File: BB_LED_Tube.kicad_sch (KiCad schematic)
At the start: 45 parts, among them U1 ESP32-WROOM-32, U2 MAX485E, U3 TPS54202DDC, U4 AP2112K-3.3

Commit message: added reverse voltage protection & more mounting holes
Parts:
- added D1: D_Small, Diode_SMD:D_SMB, symbol Device:D_Small
- added H3, H4: MountingHole, MountingHole:MountingHole_2.7mm_M2.5, symbol Mechanical:MountingHole
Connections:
- net VCC: now also D1.1 (K); no longer VCC2.1
- new net VIN: D1.2 (A), VCC2.1
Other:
- moved on the sheet: GND1, GND2, GND3, GND4, GND5, GND6, GND7, VCC1, VCC2, VCC3, VCC4, VCC5

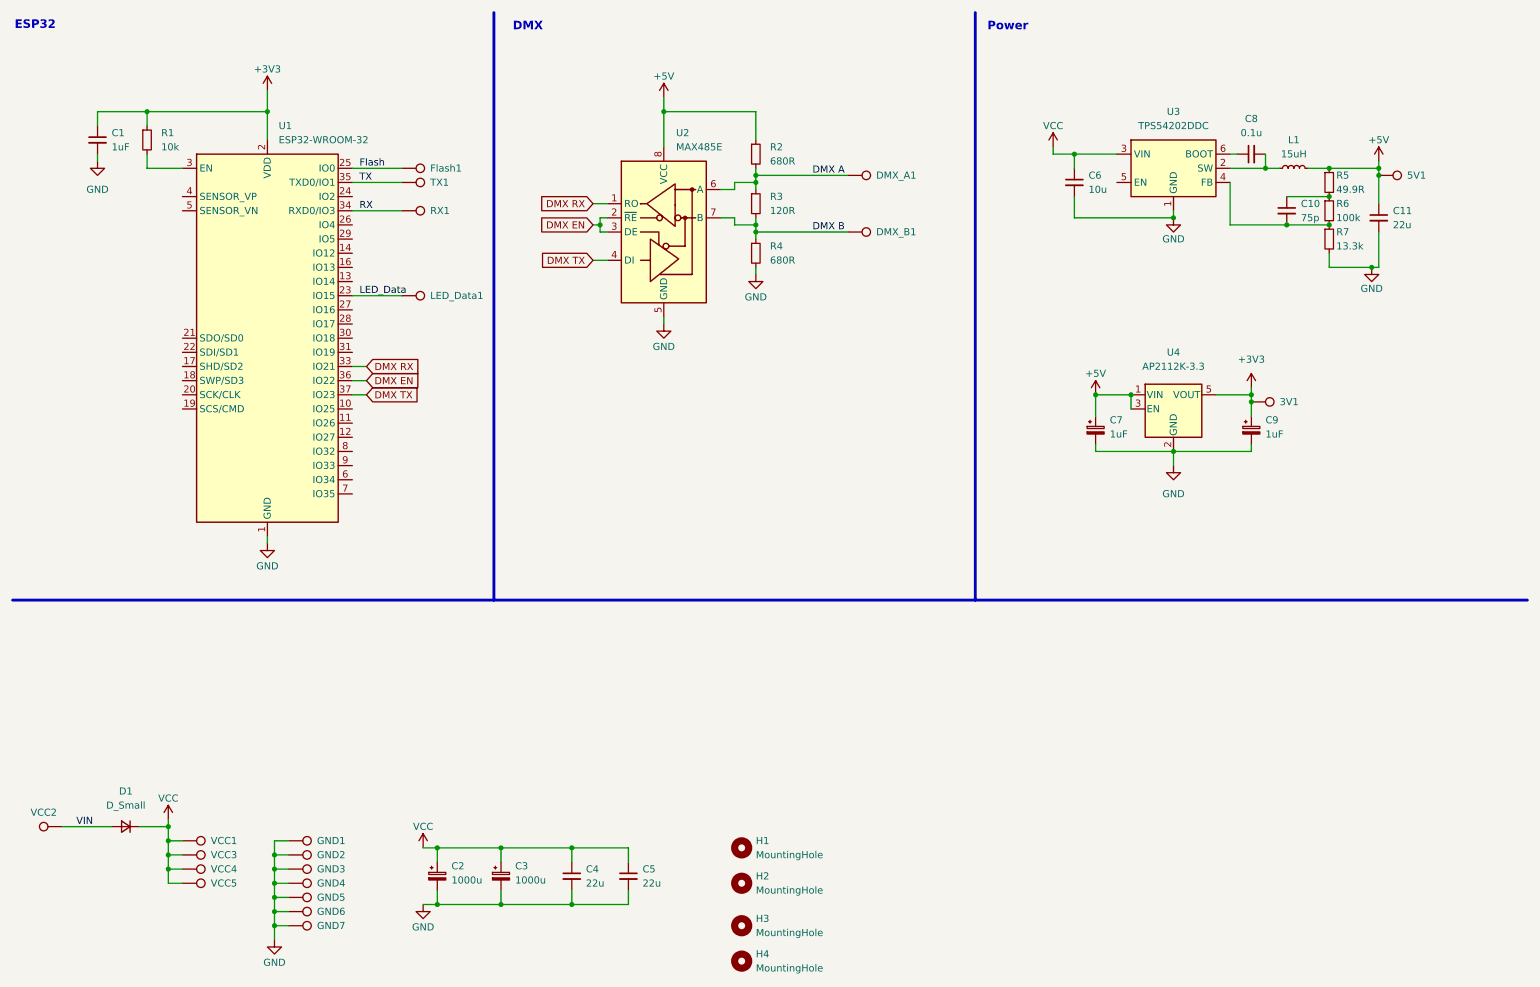
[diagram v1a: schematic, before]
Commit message: added voltage shifter and exchanged RS485 chip
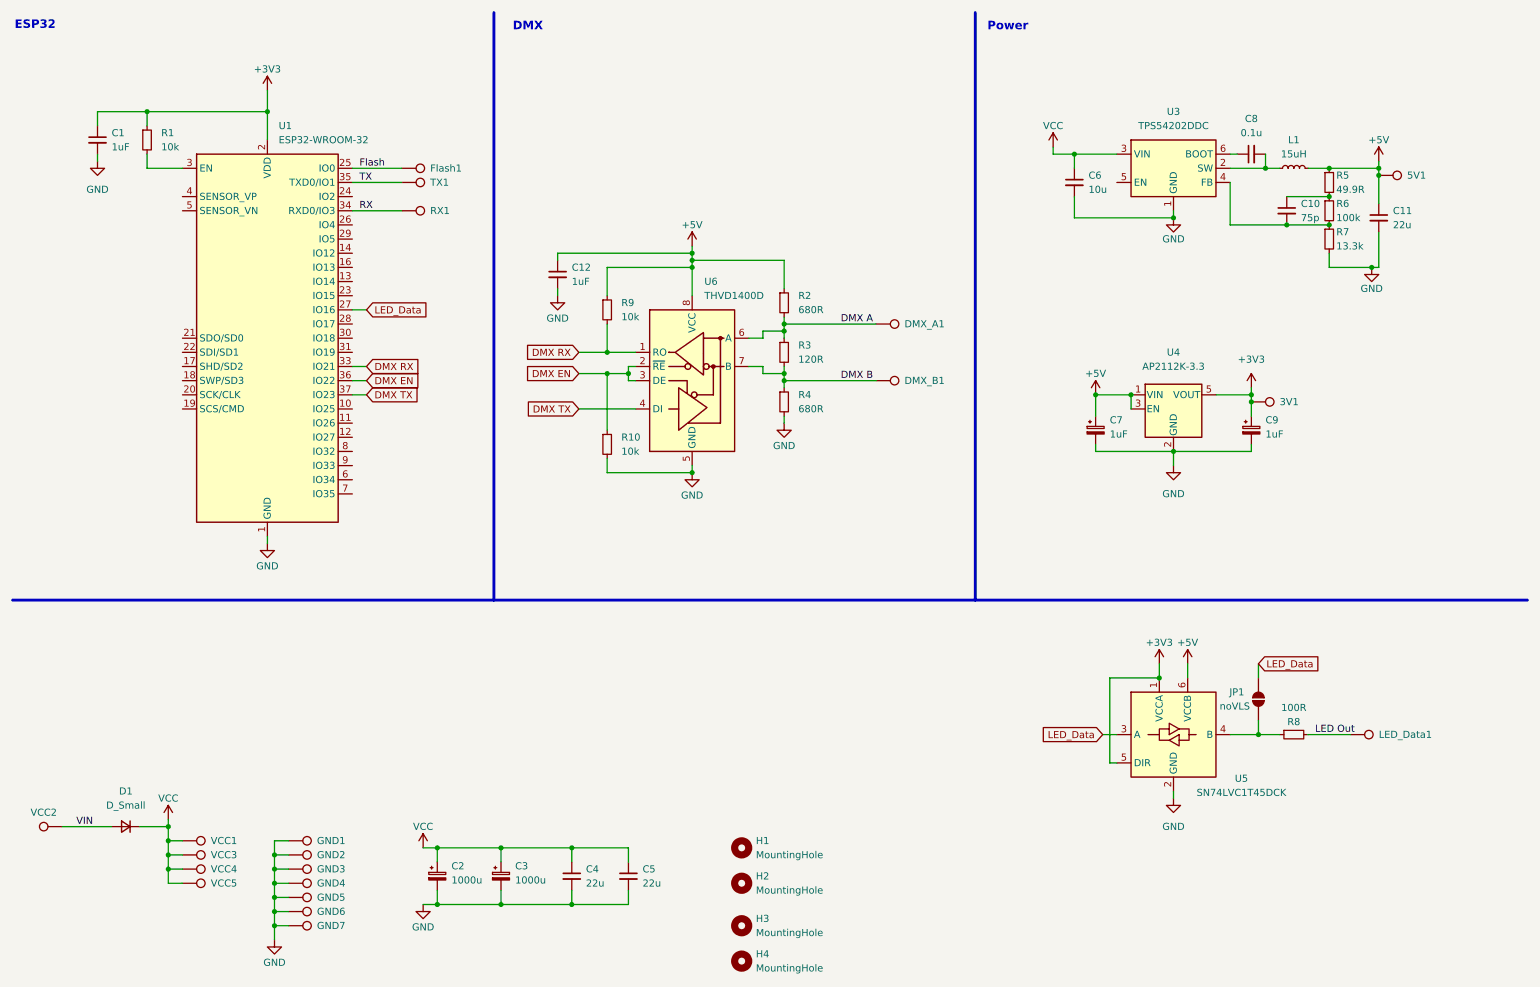
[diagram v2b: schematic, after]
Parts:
- removed U2: MAX485E, Package_SO:SOIC-8_3.9x4.9mm_P1.27mm, symbol Interface_UART:MAX485E
- added C12: 1uF, Capacitor_SMD:C_0603_1608Metric, symbol Device:C_Small
- added JP1: noVLS, Jumper:SolderJumper-2_P1.3mm_Open_RoundedPad1.0x1.5mm, symbol Jumper:SolderJumper_2_Open
- added R10, R9: 10k, Resistor_SMD:R_0603_1608Metric, symbol Device:R_Small
- added R8: 100R, Resistor_SMD:R_0603_1608Metric, symbol Device:R_Small
- added U5: SN74LVC1T45DCK, Package_TO_SOT_SMD:SOT-363_SC-70-6, symbol Logic_LevelTranslator:SN74LVC1T45DCK
- added U6: THVD1400D, Package_TO_SOT_SMD:SOT-583-8, symbol Interface_UART:THVD1400D
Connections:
- net +3V3: now also U5.1 (VCCA), U5.5 (DIR)
- net +5V: now also C12.1, R9.1, U5.6 (VCCB), U6.8 (VCC)
- net DMX A: now also U6.6 (A)
- net DMX B: now also U6.7 (B)
- net DMX EN: now also R10.1, U6.2 (~{RE}), U6.3 (DE)
- net DMX RX: now also R9.2, U6.1 (RO)
- net DMX TX: now also U6.4 (DI)
- net GND: now also C12.2, R10.2, U5.2 (GND), U6.5 (GND)
- net LED_Data: now also U1.27 (IO16), JP1.2 (B), U5.3 (A); no longer LED_Data1.1, U1.23 (IO15)
- new net: JP1.1 (A), R8.1, U5.4 (B)
- new net LED Out: LED_Data1.1, R8.2
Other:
- moved on the sheet: DMX_A1, DMX_B1, LED_Data1, R2, R3, R4
